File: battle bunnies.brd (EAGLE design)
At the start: 151.7 x 94 mm, 65 parts, among them IC1 CP2104, Q1 mmbt2222, Q2 mmbt2222, SW2 KMR2, U1 PCA9685, U2 SPX3819, U3 MCP73831T-2ACI/OT, X2 ESP-12, X4 20329

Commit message: Updating with latest routing attempt
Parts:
- removed R11, R13, R14, R17, R18, R19: 10K, SparkFun-Passives:0805
- added RN3: (no value), resistor-dil:EXB2HV
- RN1: value (none) -> 220
- moved JP4 45.4 mm to (128.0, 87.3), turned to 180 degrees
- moved JP2 44.5 mm to (129.5, 41.9), turned to 180 degrees
- moved R4 22.8 mm to (44.1, 68.3), turned to 270 degrees
- moved R16 9.67 mm to (57.1, 76.2), turned to 270 degrees
- moved RN2 3.49 mm to (90.2, 58.7)
- moved R10 1.27 mm to (57.1, 63.5)
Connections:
- removed net GPIO13: S2.B2
- net A0: now also RN3.5; no longer R19.2
- net A1: now also RN3.4; no longer R18.2
- net A2: now also RN3.3; no longer R17.2
- net A3: now also RN3.2; no longer R14.2
- net A4: now also RN3.1; no longer R13.2
- net A5: now also RN3.6; no longer R11.2
- net GND: now also RN3.11, RN3.12, RN3.13, RN3.14, RN3.15, RN3.16; no longer R11.1, R13.1, R14.1, R17.1, R18.1, R19.1
- net GPIO13/MOSI: now also S2.B2
- net PWM10: no longer RN2.6
- net PWM11: no longer RN2.5
- net PWM12: no longer RN2.4
- net PWM13: no longer RN2.3
- net PWM14: no longer RN2.2
- net PWM15: no longer RN2.1
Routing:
- net GPIO16: track 0.00 -> 118.7 mm, vias 0 -> 2
- net GPIO10: track 0.00 -> 116.3 mm, vias 0 -> 3
- net GPIO9: track 0.00 -> 107.5 mm, vias 0 -> 3
- net GPIO13/MOSI: track 0.00 -> 105.5 mm, vias 0 -> 1
- net N$18: track 0.00 -> 55.6 mm, vias 0 -> 1
- net N$24: track 0.00 -> 54.5 mm, vias 0 -> 1
- net N$23: track 0.00 -> 50.7 mm, vias 0 -> 1
- net N$16: track 0.00 -> 49.4 mm, vias 0 -> 1
- net N$19: track 0.00 -> 49.3 mm, vias 0 -> 1
- net PWM13: track 9.71 -> 54.7 mm, vias 0 -> 2
- net N$20: track 0.00 -> 42.9 mm, vias 0 -> 1
- net N$15: track 0.00 -> 41.2 mm, vias 0 -> 1
- net PWM14: track 10.4 -> 51.6 mm, vias 0 -> 2
- net DO: track 0.00 -> 40.0 mm, vias 0 -> 2
- net PWM15: track 10.9 -> 49.3 mm, vias 0 -> 2
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
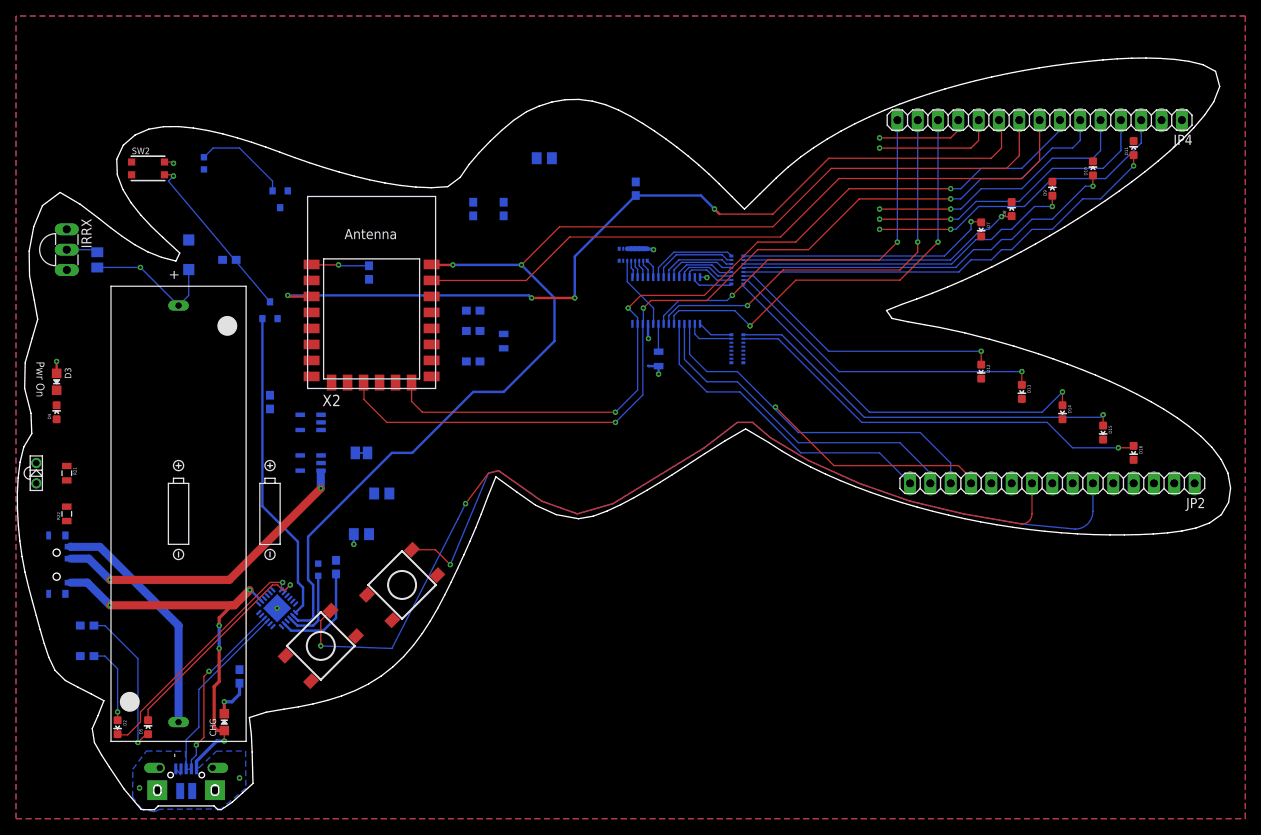
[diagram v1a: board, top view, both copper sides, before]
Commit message: Fixing ear routing
it's tighter now, but it's a lot better for obvious reasons
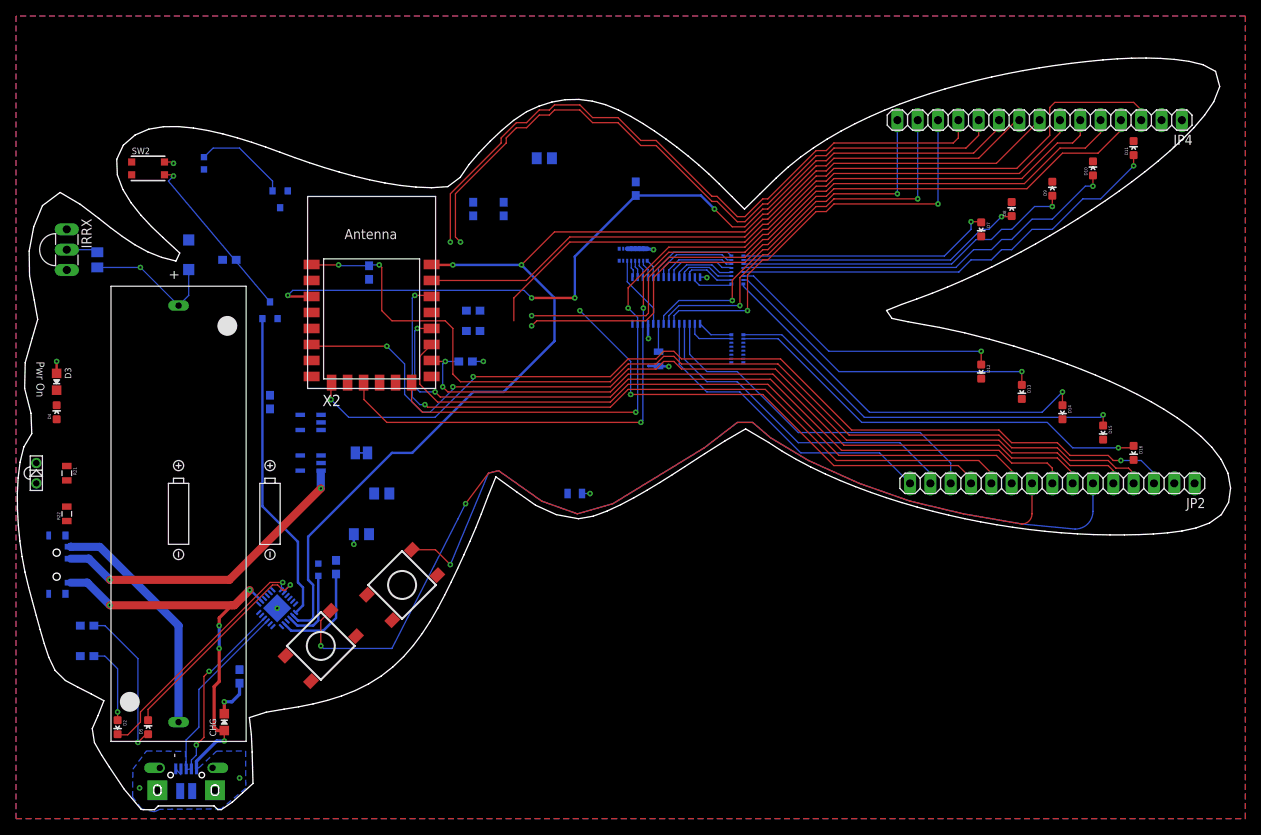
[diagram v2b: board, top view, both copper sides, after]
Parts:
- moved C1 21.0 mm to (69.8, 40.6), turned to 180 degrees
- moved R6 0.95 mm to (56.2, 57.1)
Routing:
- net CS: track 0.00 -> 117.1 mm, vias 0 -> 3
- net RESET: track 29.1 -> 145.9 mm, vias 2 -> 3
- net GPIO12/MISO: track 0.00 -> 116.0 mm, vias 0 -> 2
- net GPIO0: track 0.00 -> 96.9 mm, vias 0 -> 2
- net GPIO5/SCL: track 0.00 -> 94.4 mm, vias 0 -> 2
- net GPIO15: track 0.00 -> 93.1 mm, vias 0 -> 2
- net GPIO2: track 0.00 -> 87.5 mm
- net DI: track 11.5 -> 85.3 mm
- net CLK: track 15.3 -> 88.6 mm
- net DO: track 40.0 -> 95.1 mm, vias 2 -> 0
- net ADC: track 34.5 -> 84.8 mm, vias 2 -> 1
- net GPIO14/SCK: track 37.5 -> 87.7 mm, vias 2 -> 1
- net GPIO4/SDA: track 28.8 -> 60.9 mm, vias 1 -> 2
- net GPIO10: track 116.3 -> 120.0 mm, vias 3 -> 2
- net GPIO9: track 107.5 -> 110.7 mm, vias 3 -> 2
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
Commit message: Reworking things + the ESP12S is lacking pins present on the schematic (doh)
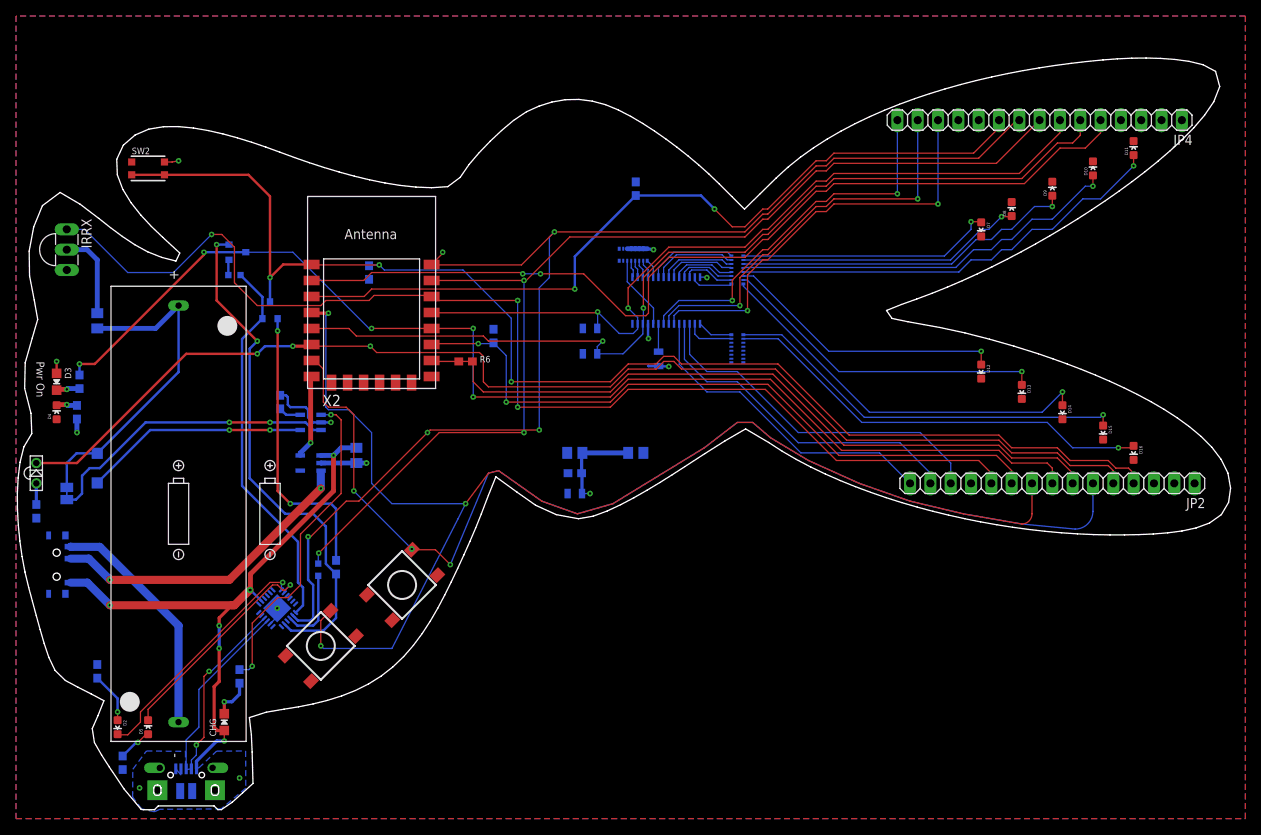
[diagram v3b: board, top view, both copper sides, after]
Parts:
- moved R22 68.4 mm to (71.8, 58.1), flipped to the bottom, turned to 0 degrees
- moved R21 67.9 mm to (71.8, 61.3), flipped to the bottom, turned to 0 degrees
- moved R23 59.1 mm to (2.54, 38.4), turned to 270 degrees
- moved R16 55.7 mm to (7.62, 50.8)
- moved R10 50.0 mm to (7.94, 54.6), turned to 270 degrees
- moved SJ1 37.2 mm to (6.35, 40.6), turned to 90 degrees
- moved C2 37.0 mm to (69.8, 45.7), turned to 180 degrees
- moved C8 35.8 mm to (77.5, 45.7)
- moved R9 34.4 mm to (59.7, 60.3), turned to 90 degrees
- moved C7 34.2 mm to (69.8, 43.2), turned to 180 degrees
- moved D1 29.0 mm to (10.2, 43.8), turned to 90 degrees
- moved R1 17.7 mm to (13.3, 6.99), turned to 90 degrees
- moved R7 14.5 mm to (27.3, 67.9), turned to 0 degrees
- moved Q2 8.58 mm to (27.6, 70.8), turned to 90 degrees
- moved C3 7.62 mm to (10.2, 62.2)
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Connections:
- removed net CLK: JP4.11, X2.20
- removed net CS: JP2.3, X2.17
- removed net DI: JP4.12, X2.21
- removed net DO: JP4.3, X2.18
- removed net GPIO10: JP4.6, R22.1, U1.26, X2.19
- removed net GPIO12: D6.C
- removed net GPIO9: JP4.7, R21.1, U1.27, X2.22
- net GPIO12/MISO: now also D6.C
- net GPIO14/SCK: now also JP4.6, R22.1, U1.26; no longer JP4.4
- net GPIO4/SDA: now also JP4.7, R21.1, U1.27; no longer JP2.12
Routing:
- net GPIO10: track 120.0 -> 0.00 mm, vias 2 -> 0
- net CS: track 117.1 -> 0.00 mm, vias 3 -> 0
- net GPIO9: track 110.7 -> 0.00 mm, vias 2 -> 0
- net DO: track 95.1 -> 0.00 mm
- net CLK: track 88.6 -> 0.00 mm, vias 1 -> 0
- net DI: track 85.3 -> 0.00 mm, vias 1 -> 0
- net VBUS: track 50.8 -> 104.9 mm, vias 5 -> 9
- net GPIO5/SCL: track 94.4 -> 146.7 mm, vias 2 -> 3
- net RXD: track 85.6 -> 137.8 mm, vias 0 -> 3
- net GPIO0: track 96.9 -> 148.9 mm, vias 2 -> 5
- net DTR: track 13.0 -> 64.7 mm, vias 0 -> 2
- net N$3: track 0.00 -> 40.7 mm, vias 0 -> 2
- net GPIO16: track 118.8 -> 159.0 mm, vias 2 -> 3
- net GPIO4/SDA: track 60.9 -> 98.5 mm
- net N$9: track 0.00 -> 37.5 mm, vias 0 -> 2
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
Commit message: Finishing up for the night, think this is all routed now
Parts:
- moved R16 11.8 mm to (4.76, 62.2), turned to 90 degrees
- moved D4 11.6 mm to (7.30, 62.2), turned to 180 degrees
- moved SJ1 10.6 mm to (9.21, 50.8), turned to 0 degrees
- moved D1 8.98 mm to (3.81, 50.2)
- moved R10 5.17 mm to (4.45, 58.4), turned to 90 degrees
- moved D3 4.41 mm to (7.30, 58.4), turned to 0 degrees
- moved S1 1.00 mm to (4.13, 31.4)
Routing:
- net VBAT: track 41.4 -> 0.08 mm
- net GND: track 82.6 -> 47.7 mm, vias 12 -> 14
- net VBUS: track 104.9 -> 115.0 mm, vias 9 -> 6
- net N$9: track 37.5 -> 29.1 mm
- net GPIO0: track 148.9 -> 154.0 mm
- net 3.3V: track 12.0 -> 13.9 mm
- net EN: track 39.0 -> 38.0 mm
- net TXD: vias 5 -> 4
- net GPIO12/MISO: vias 3 -> 2
- added copper zone on layer 16, net VBAT

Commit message: more cleanups
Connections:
- net GPIO0: now also JP2.3; no longer JP2.8
- net GPIO12/MISO: now also JP2.12; no longer JP2.5
- net GPIO2: now also JP2.4; no longer JP2.10
- net RESET: now also JP2.5; no longer JP2.4
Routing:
- net GPIO12/MISO: track 153.4 -> 134.8 mm
- net GPIO2: track 86.0 -> 97.8 mm, vias 2 -> 1
- net GPIO0: track 154.0 -> 158.7 mm, vias 5 -> 3
- net RESET: track 160.9 -> 157.6 mm
- net TXD: track 156.4 -> 154.3 mm, vias 4 -> 3
- net GPIO5/SCL: track 146.7 -> 145.0 mm
- net GND: track 47.7 -> 46.3 mm
- net GPIO15: track 90.5 -> 89.2 mm
- net CH_PD: track 101.2 -> 102.2 mm
- net GPIO14/SCK: track 116.6 -> 117.5 mm
- net ADC: track 114.9 -> 115.2 mm, vias 2 -> 0

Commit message: Finally moved things around enough to make it all work
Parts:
- removed C2: 10uF, microbuilder:0805-NO
- added U$17: AAA3, Warthog9-Batteries:AAA3
- moved C3 48.3 mm to (35.1, 20.8)
- moved R5 42.4 mm to (27.0, 71.8), turned to 180 degrees
- moved D1 41.0 mm to (36.8, 25.8), turned to 270 degrees
- moved SJ1 38.0 mm to (32.3, 20.6), turned to 270 degrees
- moved U2 33.6 mm to (3.30, 42.7)
- moved IC1 30.2 mm to (3.93, 35.5), turned to 45 degrees
- moved D3 29.8 mm to (22.1, 84.3), turned to 90 degrees
- moved R10 29.0 mm to (22.1, 81.4), turned to 0 degrees
- moved U3 23.5 mm to (31.5, 26.7), turned to 0 degrees
- moved D6 21.1 mm to (4.76, 64.1)
- moved R23 21.1 mm to (4.76, 59.4)
- moved R16 21.0 mm to (19.2, 77.5), turned to 180 degrees
- moved R8 20.8 mm to (32.4, 31.3)
- moved R12 20.5 mm to (49.2, 48.1), turned to 180 degrees
- moved S1 20.3 mm to (4.06, 51.7)
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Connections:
- net N$6 renamed USBD_P
- net N$7 renamed USBD_N
- new net +: U$17.POS
- new net -: U$17.NEG
- net 3.3V: no longer C2.1
- net GND: no longer C2.2
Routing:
- net USB_RX: track 9.97 -> 51.0 mm, vias 0 -> 2
- net N$12: track 36.2 -> 5.77 mm, vias 2 -> 0
- net N$9: track 29.1 -> 4.68 mm, vias 2 -> 0
- net TXD: track 154.3 -> 177.3 mm, vias 3 -> 4
- net VBAT: track 0.08 -> 22.8 mm, vias 0 -> 1
- net EN: track 38.0 -> 16.3 mm, vias 2 -> 0
- net GPIO16: track 159.2 -> 137.9 mm, vias 3 -> 2
- net N$3: track 40.7 -> 20.4 mm
- net VBUS: track 115.0 -> 98.2 mm, vias 6 -> 5
- net DTR: track 64.7 -> 49.3 mm, vias 2 -> 0
- net RXD: track 137.8 -> 122.5 mm, vias 3 -> 2
- net GND: track 46.3 -> 31.1 mm, vias 14 -> 17
- net USBD_N: track 22.8 -> 37.5 mm
- net USBD_P: track 22.7 -> 37.3 mm
- net GPIO14/SCK: track 117.5 -> 131.4 mm, vias 2 -> 5
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- added copper zone on layer 16, net VBUS
- removed copper zone on layer 16, net VBAT

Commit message: Just adding some silk
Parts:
- removed U$17: AAA3, Warthog9-Batteries:AAA3
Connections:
- removed net +: U$17.POS
- removed net -: U$17.NEG
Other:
- board text added: "(C) John 'Warthog9' Hawley 2016 CC-BY-SA Artwork by Dr. Terri Oda"
- board text added: "Battle Bunnies v0.9"
- board text added: "Battle!"
- board text added: "Chg"
- board text added: "GPIO0 LED"
- board text added: "Health"
- board text added: "Level"
- board text added: "Magic"
- board text added: "Reset"
- board text added: "Rx"
- board text added: "TX"
- board text added: "This is intended as a fun badge toy to play with. It was designed for PyCon Pune India, February 2017. Go, play with others and see what comes of it! - John & Terri"
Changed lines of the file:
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@@
 <wire x1="0.757" y1="32.7676" x2="1.1207" y2="30.82978125" width="0.025" layer="20"/>
 <wire x1="1.1207" y1="30.82978125" x2="1.58071875" y2="28.9129" width="0.025" layer="20"/>
-<text x="20.47875" y="78.4225" size="1.016" layer="21" font="vector" rot="SR180">Pwr On</text>
+<text x="21.21535" y="78.5241" size="1.016" layer="21" font="vector" rot="SR180">Pwr On</text>
 <rectangle x1="22.63648125" y1="-0.03175" x2="23.27401875" y2="0.03175" layer="201"/>
 <rectangle x1="22.44851875" y1="0.03175" x2="23.58898125" y2="0.09525" layer="201"/>
@@
 <rectangle x1="137.82801875" y1="95.21825" x2="144.04848125" y2="95.28175" layer="201"/>
 <rectangle x1="139.28598125" y1="95.28175" x2="142.84451875" y2="95.34525" layer="201"/>
+<text x="68.58" y="52.07" size="1.016" layer="22" rot="MR90">(C) John 'Warthog9' Hawley 2016
+CC-BY-SA
+Artwork by Dr. Terri Oda</text>
+<text x="80.01" y="83.82" size="2.54" layer="22" rot="MR270">Battle Bunnies v0.9</text>
+<text x="53.34" y="77.47" size="1.016" layer="22" rot="MR270">This is intended as a fun badge toy to play with.
+It was designed for PyCon Pune India, February 2017.
+Go, play with others and see what comes of it!
+- John &amp; Terri</text>
+<text x="116.84" y="76.2" size="1.016" layer="21" rot="SR270">Health</text>
+<text x="116.84" y="58.42" size="1.016" layer="21" rot="SR270">Level</text>
+<text x="45.72" y="34.29" size="1.016" layer="21" rot="R45">Magic</text>
+<text x="38.1" y="25.4" size="1.016" layer="21" rot="R45">Battle!</text>
+<text x="20.32" y="80.01" size="1.016" layer="21">Reset</text>
+<text x="24.3332" y="10.9982" size="1.016" layer="21">Chg</text>
+<text x="7.62" y="25.4" size="0.8128" layer="21" rot="SR270">TX</text>
+<text x="7.62" y="21.59" size="0.8128" layer="21" rot="SR270">Rx</text>
+<text x="20.5486" y="81.3562" size="0.8128" layer="21">GPIO0 LED</text>
 </plain>
 <attributes>
@@
 <attribute name="MF" value="" x="89.8525" y="69.215" size="0.17018125" layer="28" rot="MR0" display="off"/>
 </element>
-<element name="U$17" library="Warthog9-Batteries" package="AAA3" value="AAA3" x="25.7175" y="43.4975" rot="MR270"/>
 </elements>
 <signals>
@@
 <wire x1="4.7625" y1="62.865" x2="4.7625" y2="60.2225" width="0.4064" layer="16"/>
 </signal>
-<signal name="-">
-<contactref element="U$17" pad="NEG"/>
-</signal>
-<signal name="+">
-<contactref element="U$17" pad="POS"/>
-</signal>
 </signals>
 <errors>
@@
 </board>
 </drawing>
+<compatibility>
+<note version="6.3" minversion="6.2.2" severity="warning">
+Since Version 6.2.2 text objects can contain more than one line,
+which will not be processed correctly with this version.
+</note>
+</compatibility>
 </eagle>
